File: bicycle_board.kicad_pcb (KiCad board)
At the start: 2 copper layers, 41.4 x 84.9 mm, 130 parts, among them J1 Micro_SD_Card, J10 USB_A, J12 Conn_01x04, J13 Conn_01x04, J2 USB_C_Receptacle_USB2.0_16P, J3 Conn_01x02, J4 Conn_01x02, J6 Conn_01x08, J7 Conn_01x05, J8 Conn_01x02, J9 Conn_01x06, Q1 Q_NMOS_GSD, Q2 Q_NMOS_GSD, Q3 Q_NMOS_GSD, Q4 Q_NMOS_GSD, Q5 Q_NMOS_GSD, Q6 Si2302, Q7 Si2302, Q8 Q_PMOS_GSD, U1 TP4056, U11 BMP280, U12 MMC5633NJL, U13 NS4168, U14 ESP32-C3-WROOM-02U, U15 CH32V203C8T6, U16 PS7516, U17 TXB0108PW, U2 SGM2039, U3 IIM-42652, U4 QMI8610, U5 AHT20, U6 SGM2033-1.8, U7 74HC595, U8 SGM8040-1, U9 PCA9306DC1, Y1 12MHz, Y2 32.768kHz

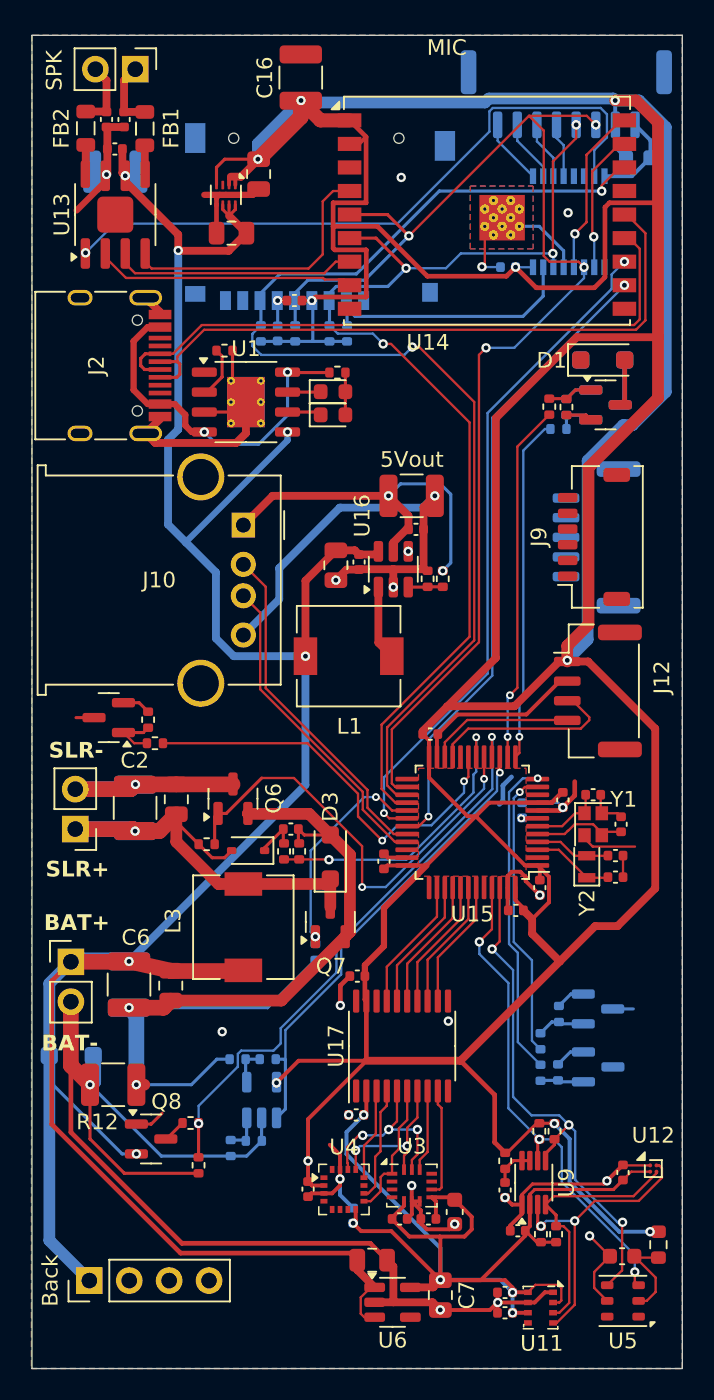
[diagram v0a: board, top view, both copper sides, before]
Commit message: 修复一些DRC错误和警告，大多数信号接口改成SH1.0接口
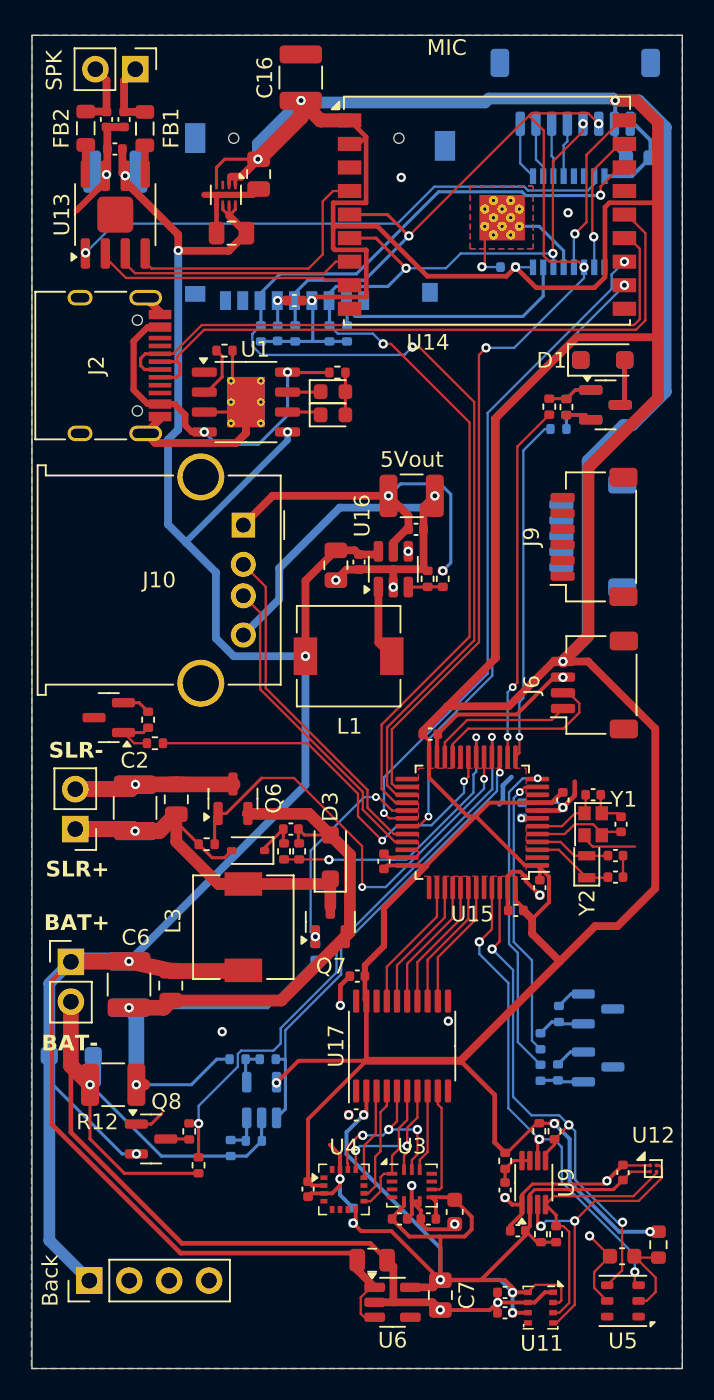
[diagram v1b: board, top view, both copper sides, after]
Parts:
- removed J12: Conn_01x04, Connector_JST:JST_GH_BM04B-GHS-TBT_1x04-1MP_P1.25mm_Vertical
- added J5: Conn_01x08, Connector_JST:JST_SH_SM08B-SRSS-TB_1x08-1MP_P1.00mm_Horizontal, B.Cu at (135.2, 60.7)
- J6: value Conn_01x08 -> Conn_01x04; footprint Connector_JST:JST_GH_BM08B-GHS-TBT_1x08-1MP_P1.25mm_Vertical -> Connector_JST:JST_SH_SM04B-SRSS-TB_1x04-1MP_P1.00mm_Horizontal; moved to F.Cu
- J7: footprint Connector_JST:JST_GH_BM05B-GHS-TBT_1x05-1MP_P1.25mm_Vertical -> Connector_JST:JST_SH_SM05B-SRSS-TB_1x05-1MP_P1.00mm_Horizontal
- J9: footprint Connector_JST:JST_SHL_SM06B-SHLS-TF_1x06-1MP_P1.00mm_Horizontal -> Connector_JST:JST_SH_SM06B-SRSS-TB_1x06-1MP_P1.00mm_Horizontal
- moved J6 37.7 mm to (136.4, 98.5), turned to 90 degrees
- moved R14 0.54 mm to (110.6, 126.9), turned to 90 degrees
- moved J7 0.26 mm to (136.3, 89.0), turned to -90 degrees
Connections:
- J6 pad 1: GND -> /SDA2
- J6 pad 2: +3.3V -> /SCL2
- J6 pad 3: /SPI_SCLK -> GND
- J6 pad 4: /SPI_MOSI -> +3.3V
- J6 pad MP: (no net) -> GND
- J7 pad MP: (no net) -> GND
- J9 pad MP: (no net) -> GND
- Q3 pad 3: Net-(D2-A) -> unconnected-(Q3-D-Pad3)
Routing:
- net /SPK_EN: track 42.2 -> 34.9 mm
- net Net-(D2-A): track 4.29 -> 2.98 mm
- net unconnected-(Q1-D-Pad3): track 1.15 -> 0.00 mm
- net /ADC_Vbat: track 37.0 -> 37.7 mm
- net /SCL2: track 12.2 -> 11.6 mm
- net /LCD_BL: track 4.20 -> 3.68 mm
- net GND: track 222.7 -> 222.3 mm, vias 23 -> 24
- net +3.3V: track 357.4 -> 357.7 mm, vias 10 -> 9

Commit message: 添加霍尔元件接口，移除CH2,CH3 MOS通道，调整和连接布线，取消STM32与ESP32的SPI连接
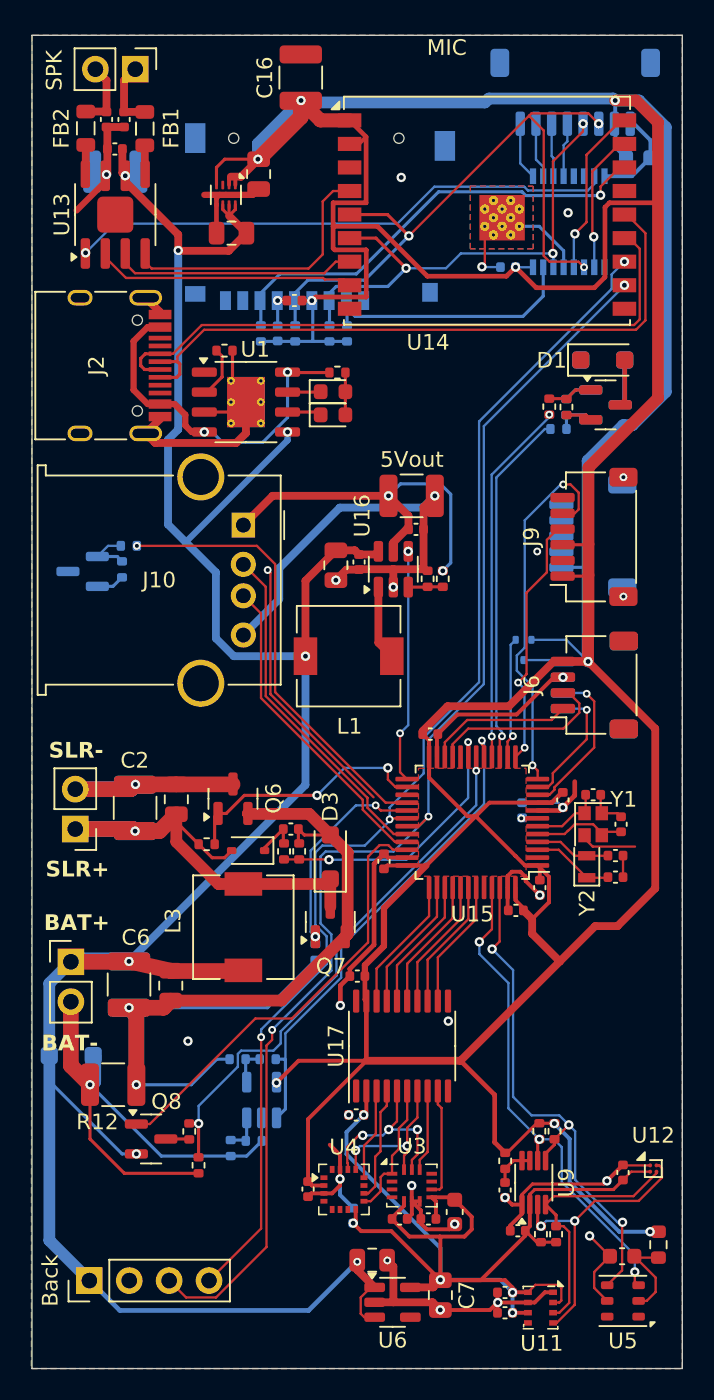
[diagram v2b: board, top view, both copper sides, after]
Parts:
- removed Q2, Q3: Q_NMOS_GSD, Package_TO_SOT_SMD:SOT-23
- removed R3, R4: R_Small, Resistor_SMD:R_0402_1005Metric
- removed R7, R8: 470, Resistor_SMD:R_0402_1005Metric
- added J11: Conn_01x04, Connector_JST:JST_SH_SM04B-SRSS-TB_1x04-1MP_P1.00mm_Horizontal, B.Cu at (136.4, 98.5)
- added Q9: Q_PMOS_GSD, Package_TO_SOT_SMD:SOT-523, B.Cu at (131.9, 96.2)
- Q1, R1, R2: moved to B.Cu
- moved R2 12.7 mm to (106.8, 89.6)
- moved R1 9.72 mm to (106.3, 91.1), turned to -90 degrees
- moved Q1 9.46 mm to (103.8, 91.2)
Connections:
- J7 pad 1: unconnected-(J7-Pin_1-Pad1) -> /I2SI_WS
- J7 pad 2: unconnected-(J7-Pin_2-Pad2) -> /I2SI_BCK
- J7 pad 3: /I2SI_WS -> /I2SI_SD
- J7 pad 4: /I2SI_BCK -> GND
- J7 pad 5: /I2SI_SD -> +3.3V
- J9 pad 1: Net-(J9-Pin_1) -> +3.3V
- J9 pad 3: Net-(J9-Pin_1) -> +3.3V
- J9 pad 4: unconnected-(J9-Pin_4-Pad4) -> /ZW101_TX
- J9 pad 5: unconnected-(J9-Pin_5-Pad5) -> /ZW101_RX
- J9 pad 6: unconnected-(J9-Pin_6-Pad6) -> GND
- U15 pad 10: unconnected-(U15-PA0-Pad10) -> /HALL1
- U15 pad 11: /CH3 -> /HALL2
- U15 pad 12: /CH2 -> /ZW101_RX
- U15 pad 13: /CH5 -> /ZW101_TX
- U15 pad 14: /CH4 -> /HALL_EN
- U15 pad 15: /ADC_Isolar -> /CH5
- U15 pad 16: /ADC_Vbat -> /CH4
- U15 pad 17: /PWM_solar -> /ADC_Isolar
- U15 pad 18: /ADC_Vsolar -> /ADC_Vbat
- U15 pad 19: /CH1 -> /ADC_Vsolar
- U15 pad 25: unconnected-(U15-PB12-Pad25) -> /5VOUT_EN
- U15 pad 26: /SPI_SCLK -> /PWM_solar
- U15 pad 27: /SPI_MISO -> unconnected-(U15-PB14-Pad27)
- U15 pad 28: /SPI_MOSI -> /CH1
- U15 pad 34: unconnected-(U15-PA13-Pad34) -> /batsamp_en
- U15 pad 37: unconnected-(U15-PA14-Pad37) -> /QMI_INT1_3V3
- U16 pad 4: /power/5VOUT_EN -> /5VOUT_EN
- U17 pad 18: /sensors/QMI_INT1_3V3 -> /QMI_INT1_3V3
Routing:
- net /SPI_MISO: track 74.9 -> 29.1 mm, vias 2 -> 1
- net /RXD: track 40.6 -> 83.4 mm, vias 2 -> 3
- net /SPI_SCLK: track 82.9 -> 42.9 mm, vias 4 -> 3
- net /SPI_MOSI: track 70.8 -> 31.7 mm, vias 4 -> 3
- net /TXD: track 43.1 -> 79.4 mm, vias 2 -> 3
- net /batsamp_en: track 1.92 -> 27.9 mm
- net /ZW101_RX: track 0.00 -> 24.0 mm, vias 0 -> 2
- net +3.3V: track 357.7 -> 335.0 mm
- net /CH2: track 20.4 -> 0.00 mm, vias 1 -> 0
- net /CH3: track 18.5 -> 0.00 mm, vias 1 -> 0
- net /ZW101_TX: track 0.00 -> 16.3 mm, vias 0 -> 2
- net /5VOUT_EN: track 0.00 -> 14.9 mm, vias 0 -> 2
- net +BATT: track 179.4 -> 164.7 mm, vias 6 -> 7
- net /PWM_solar: track 28.9 -> 16.2 mm
- net /HALL1: track 0.00 -> 10.1 mm, vias 0 -> 1
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
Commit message: 调整STM32 GPIO使用，移除右侧MOS通道，只在左侧底部保留2个，计划采用PCA9555/TCA9555 GPIO扩展芯片
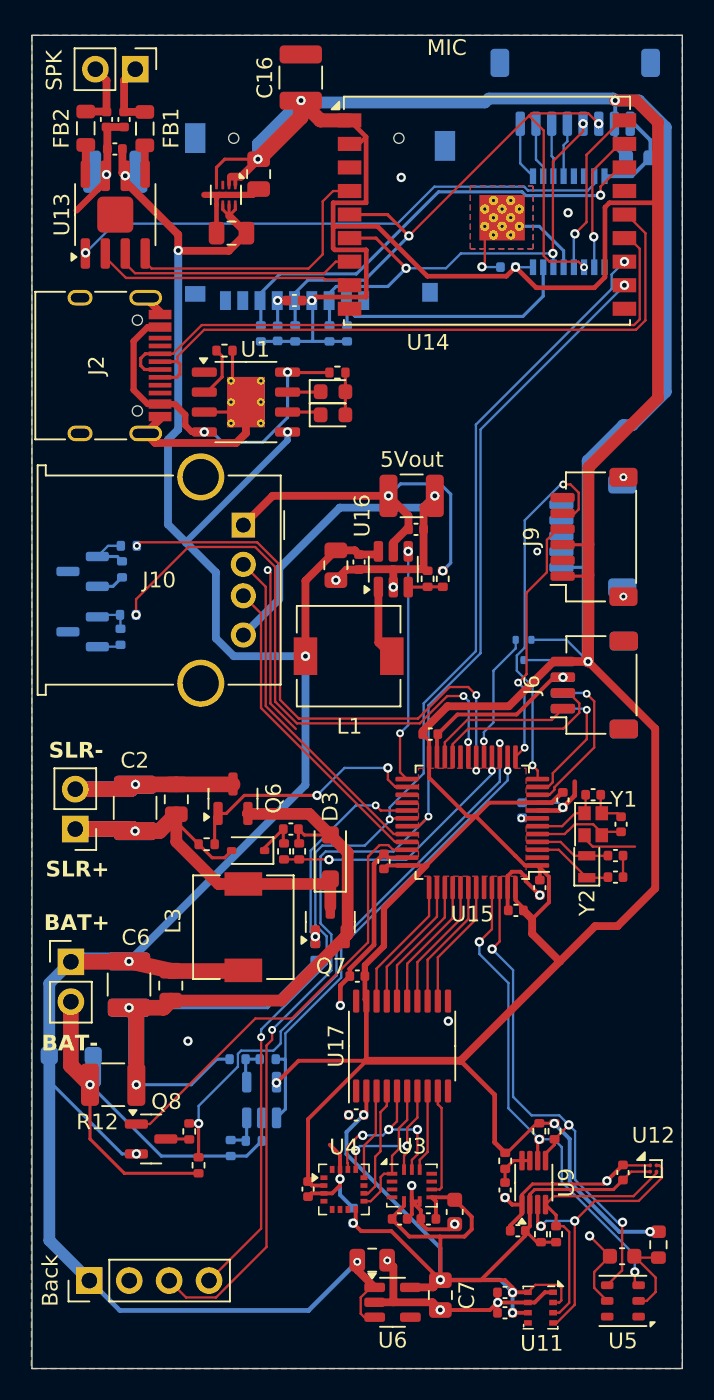
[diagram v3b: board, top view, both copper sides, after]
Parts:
- removed D1, D2: D, Diode_SMD:D_SOD-123F
- removed Q5: Q_NMOS_GSD, Package_TO_SOT_SMD:SOT-23
- removed R10: 470, Resistor_SMD:R_0402_1005Metric
- removed R6: R_Small, Resistor_SMD:R_0402_1005Metric
- Q4, R5, R9: moved to B.Cu
- moved Q4 36.3 mm to (103.8, 95.1), turned to 180 degrees
- moved R5 31.9 mm to (106.2, 95.4)
- moved R9 29.9 mm to (106.7, 94.0), turned to 180 degrees
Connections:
- Q4 pad 3: Net-(D1-A) -> unconnected-(Q4-D-Pad3)
- R9 pad 1: /CH4 -> /CH2
- U15 pad 14: /HALL_EN -> /ADC_Isolar
- U15 pad 15: /CH5 -> /ADC_Vbat
- U15 pad 16: /CH4 -> /ADC_Vsolar
- U15 pad 17: /ADC_Isolar -> /HALL_EN
- U15 pad 18: /ADC_Vbat -> /CH1
- U15 pad 19: /ADC_Vsolar -> /CH2
- U15 pad 28: /CH1 -> unconnected-(U15-PB15-Pad28)
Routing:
- net /CH2: track 0.00 -> 36.7 mm, vias 0 -> 3
- net /CH4: track 23.3 -> 0.00 mm, vias 2 -> 0
- net /CH5: track 22.7 -> 0.00 mm, vias 1 -> 0
- net /CH1: track 28.8 -> 38.1 mm, vias 1 -> 3
- net GND: track 218.4 -> 212.0 mm
- net Net-(D2-A): track 2.98 -> 0.00 mm
- net Net-(D1-A): track 2.98 -> 0.00 mm
- net Net-(Q5-G): track 2.58 -> 0.00 mm
- net /ADC_Vbat: track 34.7 -> 37.0 mm
- net Net-(Q5-S): track 1.80 -> 0.00 mm
- net /ADC_Isolar: track 31.3 -> 29.7 mm
- net /HALL_EN: track 7.79 -> 8.30 mm

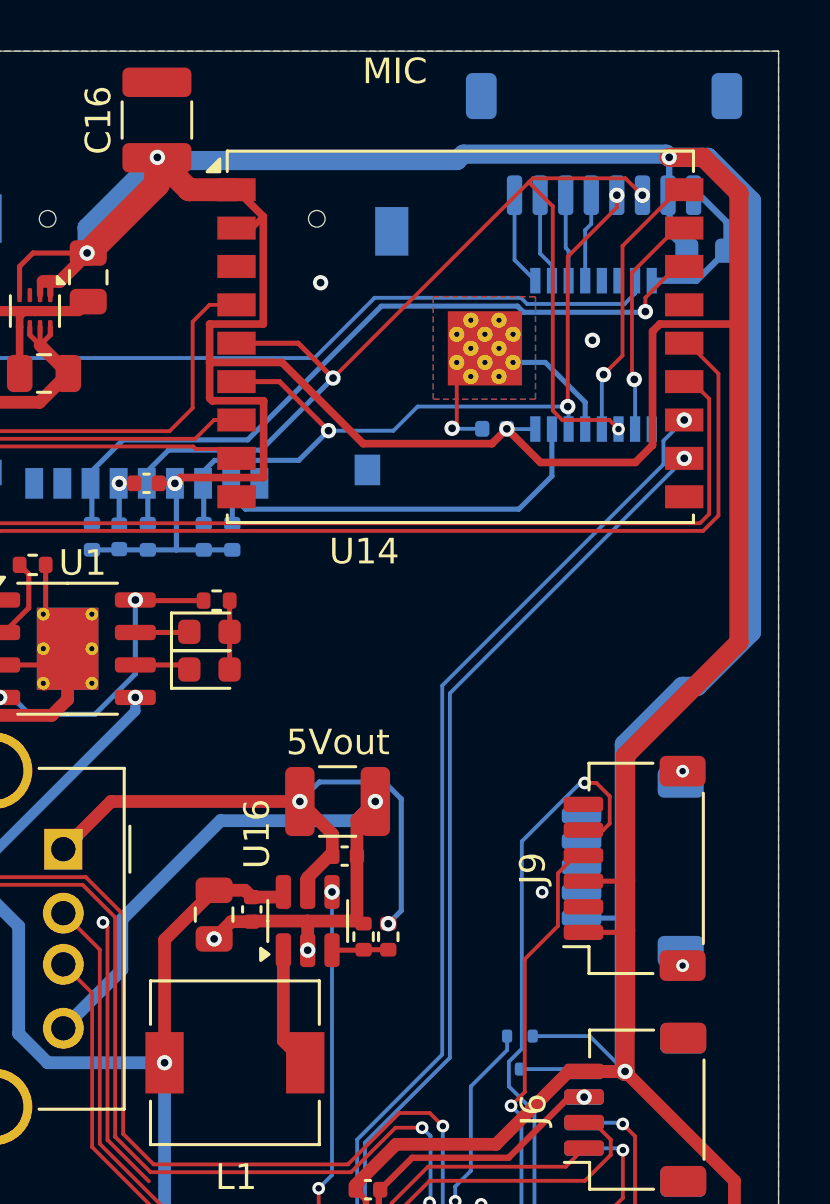
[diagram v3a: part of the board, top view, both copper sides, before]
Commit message: 连接ESP32和I2S麦克风接口
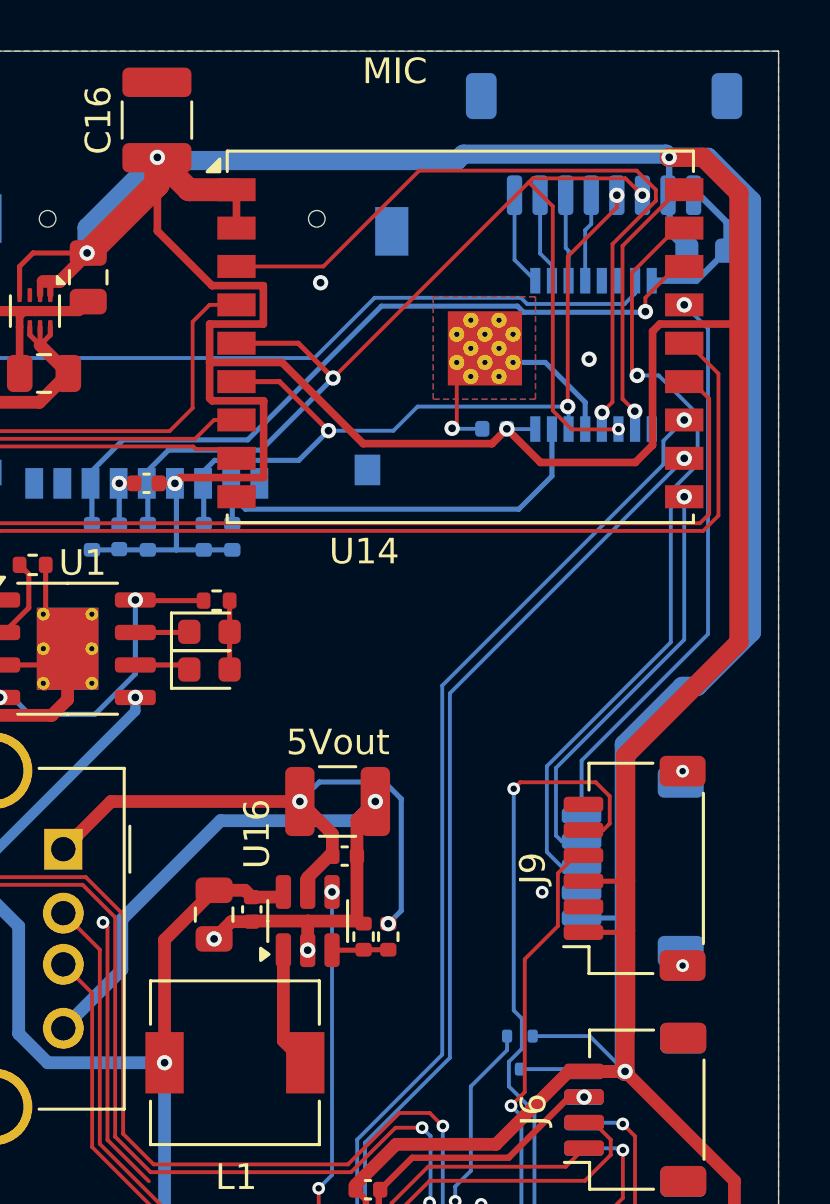
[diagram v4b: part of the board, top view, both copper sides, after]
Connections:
- J7 pad 1: /I2SI_WS -> /I2SI_SD
- J7 pad 3: /I2SI_SD -> /I2SI_WS
- U14 pad 10: unconnected-(U14-IO10-Pad10) -> /I2SI_BCK
- U14 pad 15: unconnected-(U14-IO3-Pad15) -> /I2SI_SD
- U14 pad 17: /595_CLR -> /I2SI_WS
- U14 pad 18: /595_RCLK -> /595_CLR
- U14 pad 3: unconnected-(U14-IO4-Pad3) -> /595_RCLK
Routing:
- net /I2SI_WS: track 0.00 -> 31.0 mm, vias 0 -> 1
- net /I2SI_SD: track 0.00 -> 22.4 mm, vias 0 -> 1
- net /595_RCLK: track 10.8 -> 28.5 mm
- net /I2SI_BCK: track 0.00 -> 16.4 mm, vias 0 -> 1
- net +3.3V: track 335.0 -> 339.0 mm
- net /595_CLR: track 8.93 -> 10.7 mm
- net /ZW101_RX: track 24.0 -> 25.7 mm
